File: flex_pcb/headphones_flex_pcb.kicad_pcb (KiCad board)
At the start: 2 copper layers, 41.7 x 25.7 mm, 34 parts, among them J1 LIGHTING_JACK, J2 CONN_01X01, J3 BOTTOM_FLEX_LIGHTNING, J5 LIGHTNING_HEADPHONE_ADAPTER, J7 IPHONE_HEADPHONE_JACK, U1 SN74LVC1G123, U2 SN74LVC1G123, U3 NC7S32-micropak6, U4 TS3Y5018RSV-UQFN

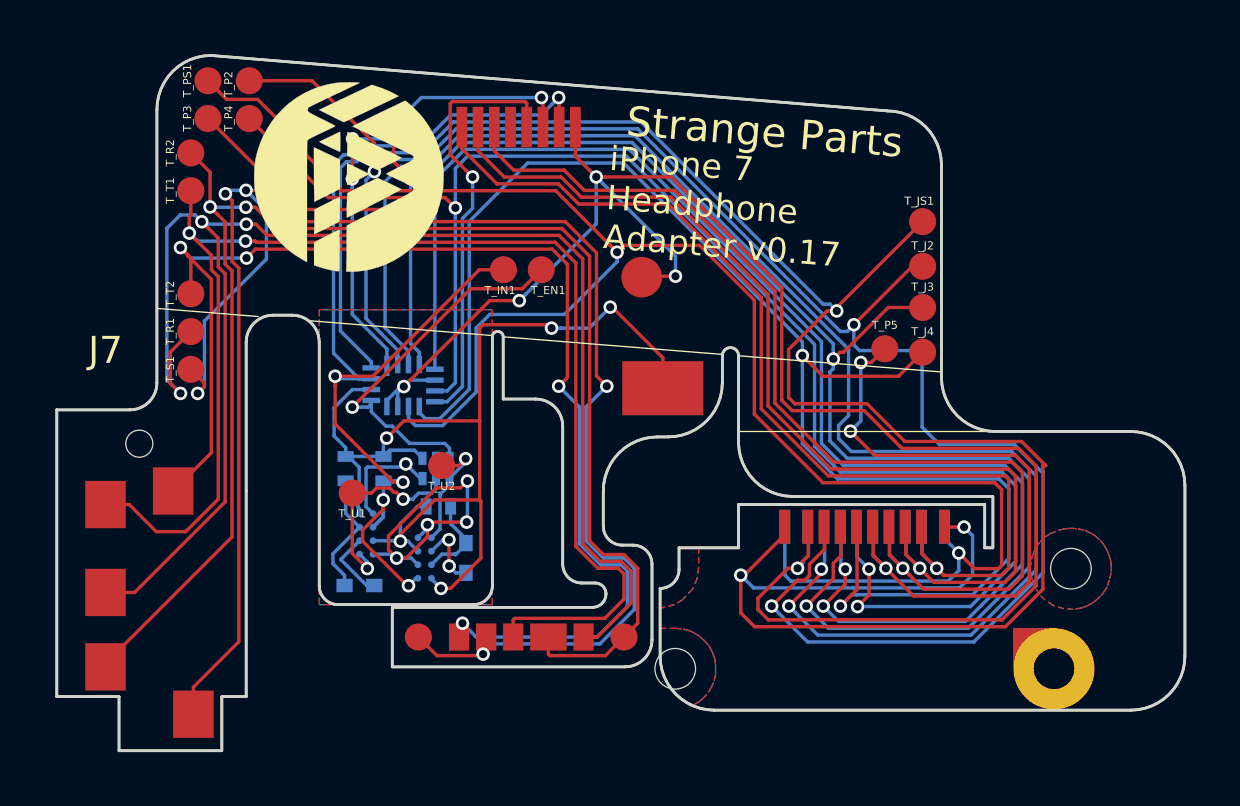
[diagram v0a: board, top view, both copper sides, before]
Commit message: Made tab with lighting pads slightly longer.
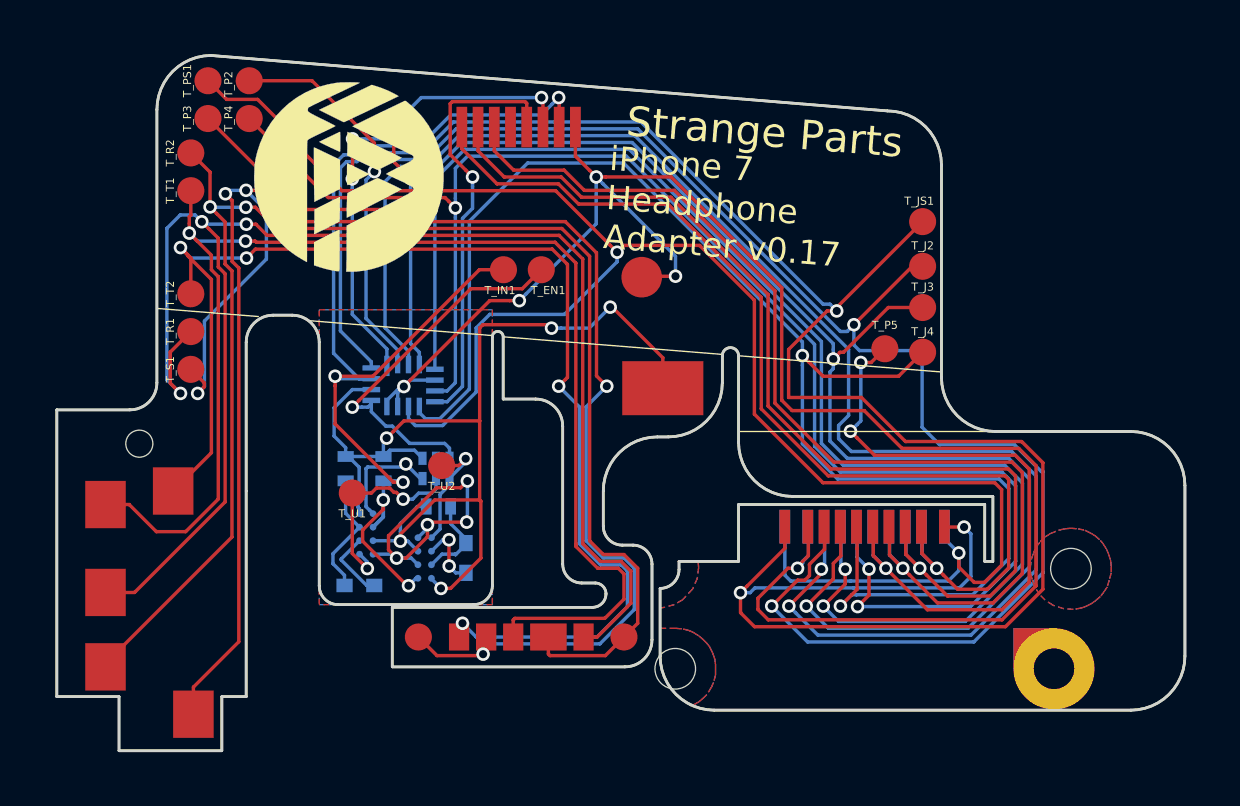
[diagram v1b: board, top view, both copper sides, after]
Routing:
- net /PSHIELD: track 65.9 -> 66.6 mm
- net /JSHIELD: track 105.3 -> 104.8 mm
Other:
- outline, holes or cut-outs redrawn

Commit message: Tweaks after v0.17
-Remove copper pours on IC area
-Fix misnumbered pads on micropak6
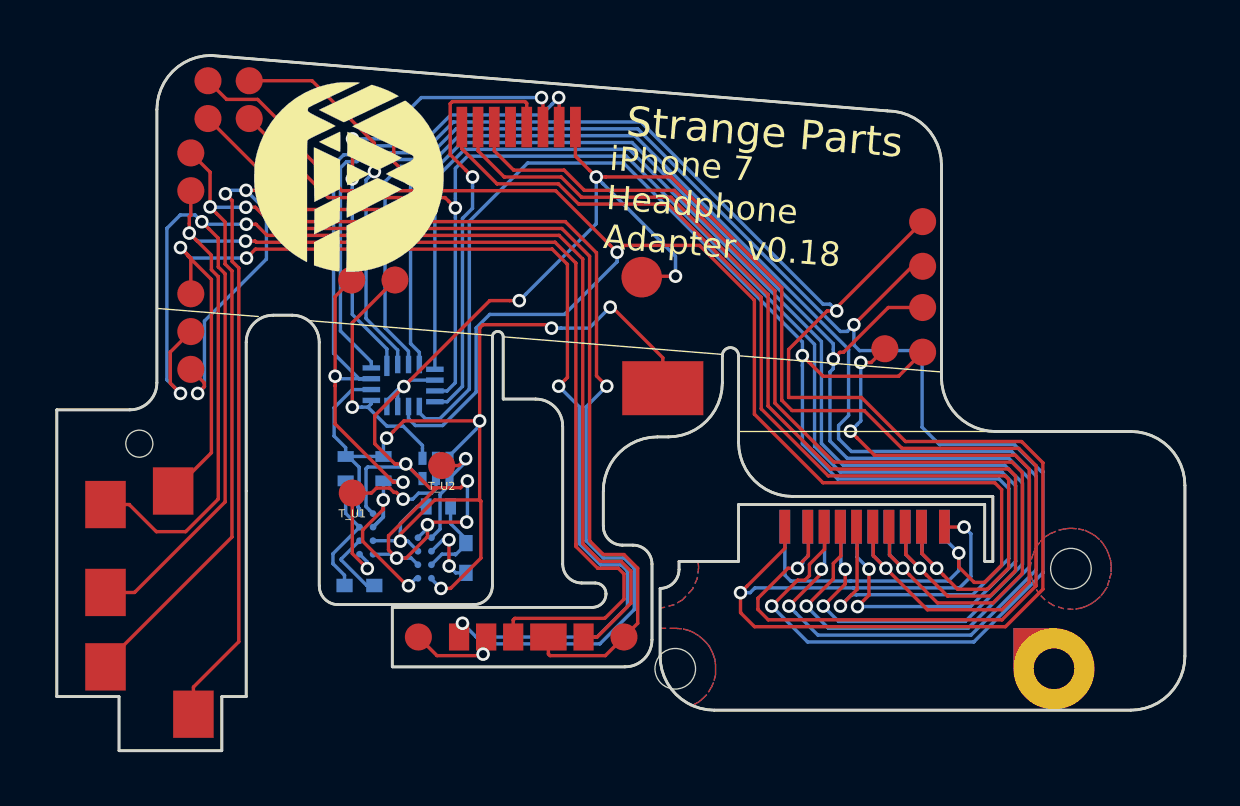
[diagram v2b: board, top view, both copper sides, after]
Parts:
- moved T_IN1 5.62 mm to (133.7, 69.1)
- moved T_EN1 5.42 mm to (135.3, 69.1)
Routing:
- net GNDREF: track 83.4 -> 88.9 mm
- net Net-(T_EN1-Pad1): track 14.1 -> 9.31 mm
- net /JSHIELD: track 104.8 -> 100.8 mm
- net VCC: track 41.2 -> 41.4 mm, vias 5 -> 6
- removed copper zone on B.Cu, net GNDREF
- removed copper zone on F.Cu, net GNDREF
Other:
- board text added: "iPhone 7 Headphone Adapter v0.18"
- board text removed: "iPhone 7 Headphone Adapter v0.17"

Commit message: Zigzag attempt 1
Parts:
- moved T_T2 5.33 mm to (123.5, 66.4)
- moved T_R1 5.10 mm to (123.5, 68.2)
- moved T_S1 4.86 mm to (123.2, 70.7)
- moved J7 0.60 mm to (125.2, 83.4)
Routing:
- net Net-(J5-Pad12): track 55.5 -> 65.0 mm
- net Net-(J5-Pad15): track 48.4 -> 55.0 mm
- net Net-(J5-Pad13): track 50.3 -> 56.5 mm
- net Net-(J5-Pad11): track 58.0 -> 57.3 mm, vias 3 -> 2
- net Net-(J5-Pad14): track 69.6 -> 69.4 mm, vias 5 -> 4
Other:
- board size 41.7 x 25.7 mm -> 41.1 x 25.7 mm

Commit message: Tweak edges and silkscreens
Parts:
- moved T_R1 10.6 mm to (134.0, 69.9)
- moved T_S1 9.67 mm to (132.8, 69.9)
- moved T_T2 4.72 mm to (127.4, 69.1)
- moved T_IN1 2.18 mm to (135.9, 69.0)
- moved T_U2 1.35 mm to (136.0, 75.1)
- moved T_EN1 1.28 mm to (135.9, 70.2)
- moved G*** 0.64 mm to (133.1, 65.7)
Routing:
- net Net-(J5-Pad11): track 57.3 -> 63.6 mm, vias 2 -> 3
- net Net-(J5-Pad13): track 56.5 -> 60.6 mm
- net Net-(J5-Pad14): track 69.4 -> 71.2 mm
- net Net-(J5-Pad15): track 55.0 -> 56.3 mm
- net Net-(T_U2-Pad1): track 4.44 -> 5.61 mm
- net /JSHIELD: track 100.8 -> 101.8 mm
- net Net-(J5-Pad12): track 65.0 -> 65.9 mm
- net Net-(T_EN1-Pad1): track 9.31 -> 8.41 mm
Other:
- outline, holes or cut-outs redrawn

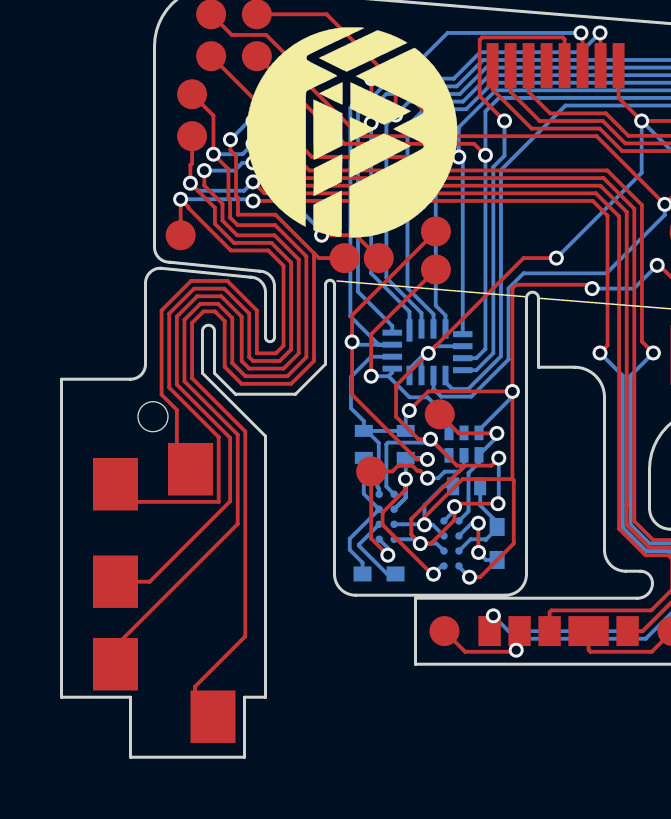
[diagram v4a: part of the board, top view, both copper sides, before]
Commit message: v0.18
- Tweak tracks into headphone jack to make them narrower.
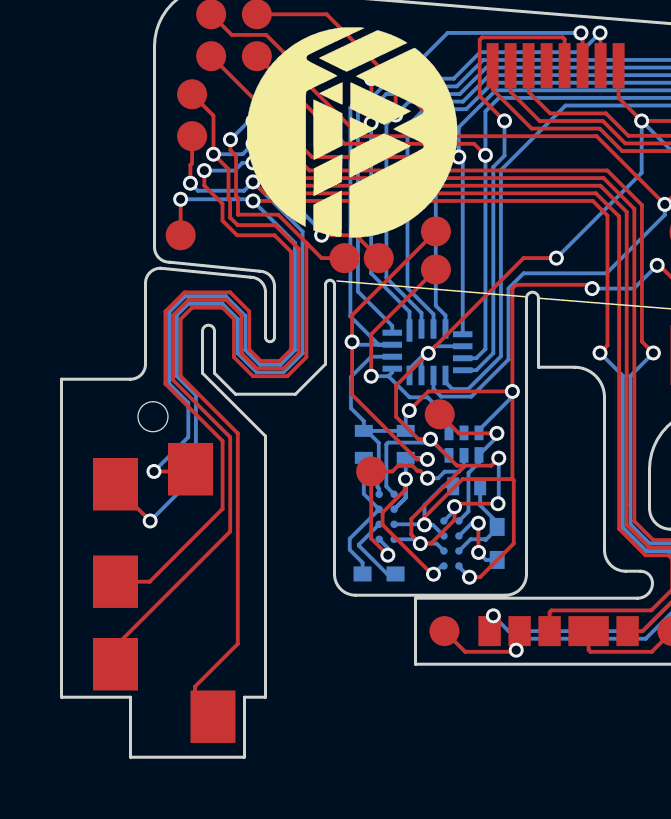
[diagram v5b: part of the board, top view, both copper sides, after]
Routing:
- net Net-(J5-Pad13): track 60.6 -> 57.3 mm, vias 2 -> 3
- net Net-(J5-Pad15): track 56.3 -> 56.4 mm, vias 4 -> 5

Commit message: v0.19
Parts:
- added G***: LOGO, 牛逼:牛逼转换器, F.Cu at (149.7, 68.3)
- moved J3 0.23 mm to (152.7, 77.8)
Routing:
- net VCC: track 41.4 -> 42.8 mm
- net GNDREF: track 88.9 -> 88.3 mm
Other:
- board text added: "Headphone Adapter v0.19"
- board text removed: "iPhone 7 Headphone Adapter v0.18"
